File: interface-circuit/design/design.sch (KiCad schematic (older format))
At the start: 3 parts

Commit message: WIP
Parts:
- removed J?: Screw_Terminal_01x04, symbol Connector:Screw_Terminal_01x04
- added J?: Conn_02x06_Counter_Clockwise, symbol Connector_Generic:Conn_02x06_Counter_Clockwise
- added J?: Conn_02x15_Counter_Clockwise, symbol Connector_Generic:Conn_02x15_Counter_Clockwise
- added J? (x2): Conn_01x02_Male, symbol Connector:Conn_01x02_Male
- added J? (x2): Screw_Terminal_01x05, symbol Connector:Screw_Terminal_01x05
- added SW? (x2): SW_SPST, symbol Switch:SW_SPST
- added U?: LogicLevelConverter_BOB-08745, symbol custom_symbols:LogicLevelConverter_BOB-08745
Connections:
- net labels added: +12V, +3V3, +5V, HV_AlarmTriggered, HV_FanPowerDemand, HV_PrinterPowerDemand, HV_PrinterPowerStatus, LV_AlarmTriggered, LV_FanPowerDemand, LV_PrinterPowerDemand, LV_PrinterPowerStatus, RESET, SOFT_SWITCH
- net labels removed: ArduinoAlarmTriggered, ArduinoPrinterPowerStatus, PiPrinterPowerDemand
- wire segments 0 -> 28
- no-connect marks 36 -> 60

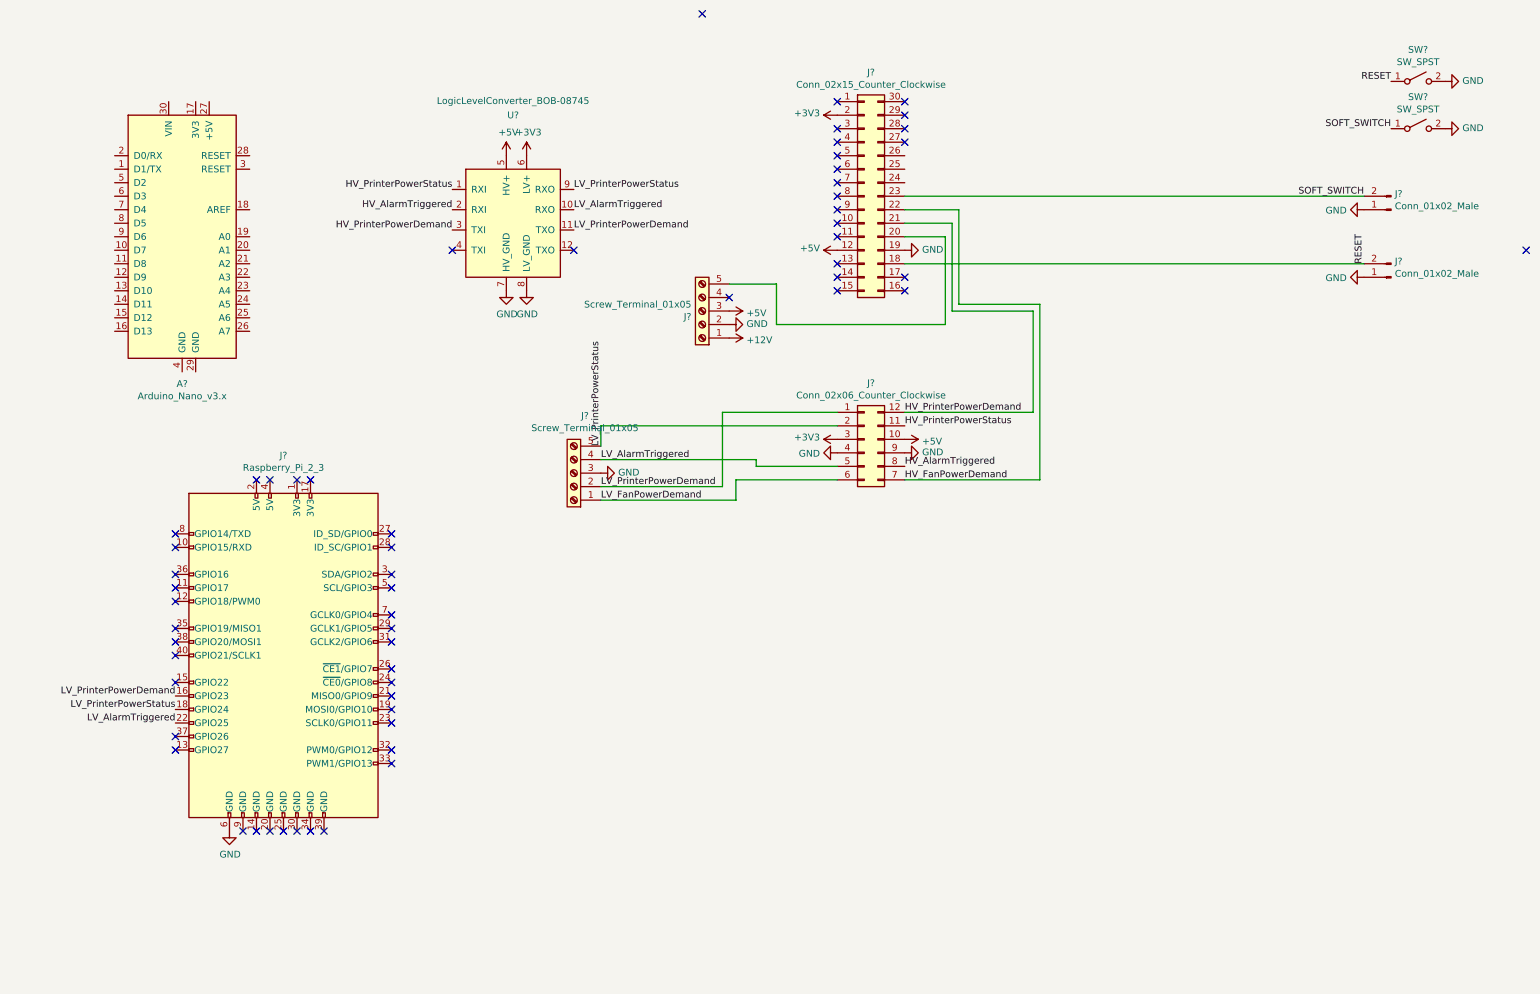
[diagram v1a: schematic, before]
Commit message: wip - transistor switches done
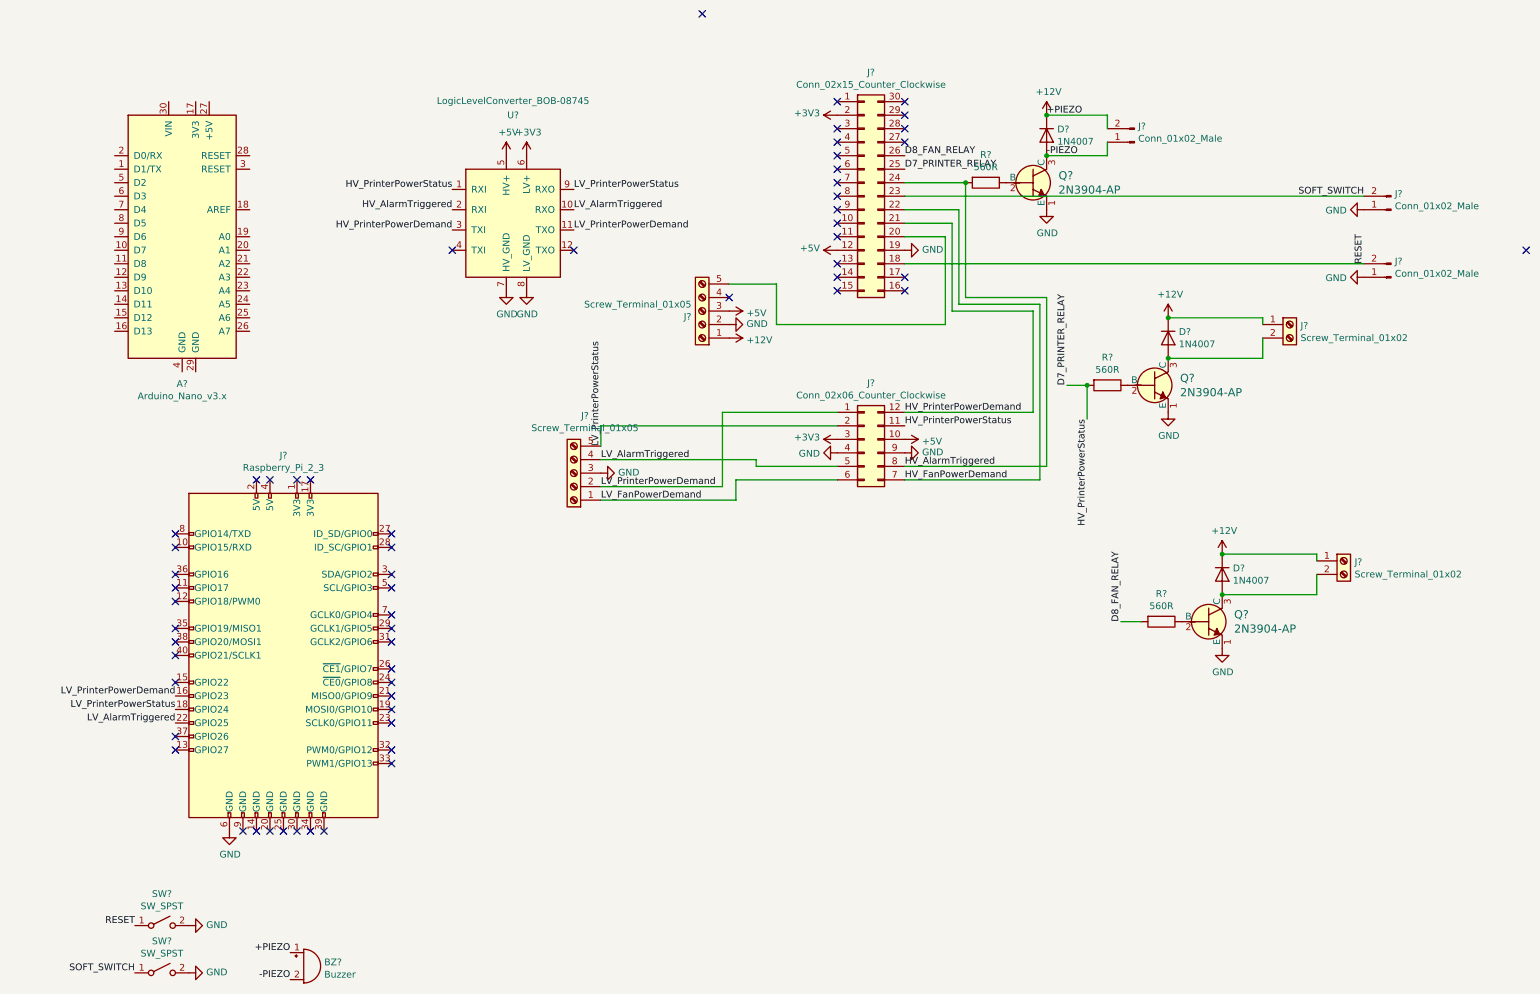
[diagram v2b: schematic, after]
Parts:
- added BZ?: Buzzer, symbol Device:Buzzer
- added D? (x3): 1N4007, Diode_THT:D_DO-41_SOD81_P10.16mm_Horizontal, symbol Diode:1N4007
- added J?: Conn_01x02_Male, symbol Connector:Conn_01x02_Male
- added J? (x2): Screw_Terminal_01x02, symbol Connector:Screw_Terminal_01x02
- added Q? (x3): 2N3904-AP, digikey-footprints:TO-92-3_Formed_Leads, symbol dk_Transistors-Bipolar-BJT-Single:2N3904-AP
- added R? (x3): 560R, symbol Device:R
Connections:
- net HV_PrinterPowerStatus is gone; now on net D7_PRINTER_RELAY: J?.11 (Pin_11), U?.1 (RXI)
- net +12V: now also BZ?.1 (-), D?.1 (K), D?.1 (K), D?.1 (K), J?.1 (Pin_1), J?.1 (Pin_1), J?.2 (Pin_2)
- net GND: now also Q?.1 (E), Q?.1 (E), Q?.1 (E)
- net HV_AlarmTriggered: now also J?.24 (Pin_24), R?.2
- net D7_PRINTER_RELAY: now reaches J?.25 (Pin_25)
- net D7_PRINTER_RELAY: now also R?.2
- net D8_FAN_RELAY: now reaches J?.26 (Pin_26)
- net D8_FAN_RELAY: now also R?.2
- new net: Q?.2 (B), R?.1 (x3)
- new net: D?.2 (A), J?.2 (Pin_2), Q?.3 (C) (x2)
- new net -PIEZO: BZ?.2 (+), D?.2 (A), J?.1 (Pin_1), Q?.3 (C)
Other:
- moved on the sheet: SW?

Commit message: Terminals for three-way switches, and 12v adaptor
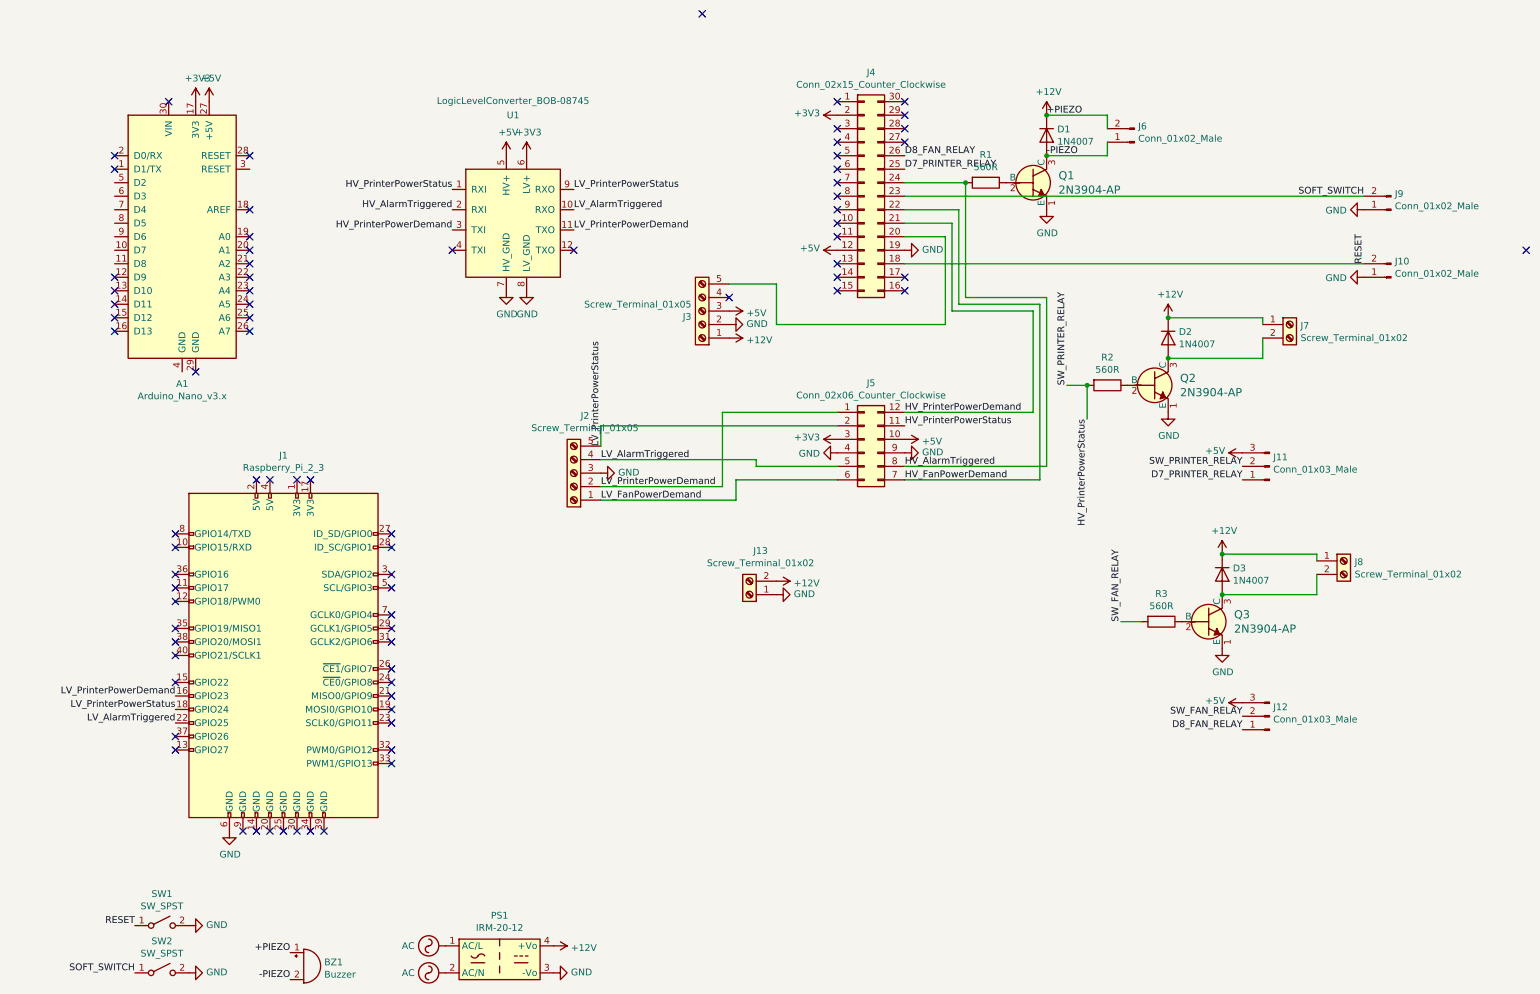
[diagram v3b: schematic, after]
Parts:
- added J11, J12: Conn_01x03_Male, symbol Connector:Conn_01x03_Male
- added J13: Screw_Terminal_01x02, symbol Connector:Screw_Terminal_01x02
- added PS1: IRM-20-12, Converter_ACDC:Converter_ACDC_MeanWell_IRM-20-xx_THT, symbol Converter_ACDC:IRM-20-12
- gave numbers to parts that had none: 24
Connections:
- net +12V: now also J13.2 (Pin_2), PS1.4 (+Vo)
- net +3V3: now also A1.17 (3V3)
- net +5V: now also A1.27 (+5V), J11.3 (Pin_3), J12.3 (Pin_3)
- net D7_PRINTER_RELAY: now also J11.1 (Pin_1); no longer J5.11 (Pin_11), R2.2, U1.1 (RXI)
- net D8_FAN_RELAY: now also J12.1 (Pin_1); no longer R3.2
- net GND: now also J13.1 (Pin_1), PS1.3 (-Vo)
- new net AC: PS1.1 (AC/L), PS1.2 (AC/N)
- new net HV_PrinterPowerStatus: J11.2 (Pin_2), J5.11 (Pin_11), R2.2, U1.1 (RXI)
- new net SW_FAN_RELAY: J12.2 (Pin_2), R3.2
- no-connect marks 60 -> 79

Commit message: Finished design and ERC passes
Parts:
- added J14: Conn_01x02_Male, symbol Connector:Conn_01x02_Male
- added R4: 220R, symbol Device:R
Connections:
- net +5V: now also R4.2
- net GND: now also A1.4 (GND), J14.1 (Pin_1)
- net HV_AlarmTriggered: now also A1.9 (D6)
- net HV_FanPowerDemand: now also A1.7 (D4)
- net HV_PrinterPowerDemand: now also A1.6 (D3)
- net HV_PrinterPowerStatus: now also A1.10 (D7)
- net RESET: now also A1.3 (RESET)
- net SOFT_SWITCH: now also A1.8 (D5)
- net SW_FAN_RELAY: now also A1.11 (D8)
- net DETECTOR_SIGNAL: now reaches A1.5 (D2)
- net DETECTOR_SIGNAL: now also J3.5 (Pin_5), J4.20 (Pin_20)
- net AC: no longer names the net of PS1.1 (AC/L)
- net AC: no longer PS1.2 (AC/N)
- new net: J14.2 (Pin_2), R4.1
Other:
- moved on the sheet: A1
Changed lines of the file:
@@
 L MCU_Module:Arduino_Nano_v3.x A1
 U 1 1 5CC13554
-P 1550 1950
-F 0 "A1" H 1550 861 50  0000 C CNN
-F 1 "Arduino_Nano_v3.x" H 1550 770 50  0000 C CNN
-F 2 "Module:Arduino_Nano" H 1700 1000 50  0001 L CNN
-F 3 "http://www.mouser.com/pdfdocs/Gravitech_Arduino_Nano3_0.pdf" H 1550 950 50  0001 C CNN
-	1    1550 1950
+P 2000 1700
+F 0 "A1" H 2000 611 50  0000 C CNN
+F 1 "Arduino_Nano_v3.x" H 2000 520 50  0000 C CNN
+F 2 "Module:Arduino_Nano" H 2150 750 50  0001 L CNN
+F 3 "http://www.mouser.com/pdfdocs/Gravitech_Arduino_Nano3_0.pdf" H 2000 700 50  0001 C CNN
+	1    2000 1700
 	1    0    0    -1
 $EndComp
@@
 $EndComp
 Connection ~ 9250 4300
-NoConn ~ 2050 1950
-NoConn ~ 2050 2050
-NoConn ~ 2050 2150
-NoConn ~ 2050 2250
-NoConn ~ 2050 2350
-NoConn ~ 2050 2450
-NoConn ~ 2050 2550
-NoConn ~ 2050 2650
-NoConn ~ 1450 950
-NoConn ~ 2050 1350
-NoConn ~ 2050 1750
-NoConn ~ 1650 2950
-NoConn ~ 1050 1350
-NoConn ~ 1050 1450
-NoConn ~ 1050 2250
-NoConn ~ 1050 2350
-NoConn ~ 1050 2450
-NoConn ~ 1050 2550
-NoConn ~ 1050 2650
+NoConn ~ 2500 1700
+NoConn ~ 2500 1800
+NoConn ~ 2500 1900
+NoConn ~ 2500 2000
+NoConn ~ 2500 2100
+NoConn ~ 2500 2200
+NoConn ~ 2500 2300
+NoConn ~ 2500 2400
+NoConn ~ 1900 700
+NoConn ~ 2500 1100
+NoConn ~ 2500 1500
+NoConn ~ 2100 2700
+NoConn ~ 1500 1100
+NoConn ~ 1500 1200
+NoConn ~ 1500 2000
+NoConn ~ 1500 2100
+NoConn ~ 1500 2200
+NoConn ~ 1500 2300
+NoConn ~ 1500 2400
 $Comp
 L power:+3V3 #PWR0127
 U 1 1 5CCA5351
-P 1650 950
-F 0 "#PWR0127" H 1650 800 50  0001 C CNN
-F 1 "+3V3" H 1665 1123 50  0000 C CNN
-F 2 "" H 1650 950 50  0001 C CNN
-F 3 "" H 1650 950 50  0001 C CNN
-	1    1650 950
+P 2100 700
+F 0 "#PWR0127" H 2100 550 50  0001 C CNN
+F 1 "+3V3" H 2115 873 50  0000 C CNN
+F 2 "" H 2100 700 50  0001 C CNN
+F 3 "" H 2100 700 50  0001 C CNN
+	1    2100 700
 	1    0    0    -1
 $EndComp
@@
 L power:+5V #PWR0128
 U 1 1 5CCA5F2D
-P 1750 950
-F 0 "#PWR0128" H 1750 800 50  0001 C CNN
-F 1 "+5V" H 1765 1123 50  0000 C CNN
-F 2 "" H 1750 950 50  0001 C CNN
-F 3 "" H 1750 950 50  0001 C CNN
-	1    1750 950
+P 2200 700
+F 0 "#PWR0128" H 2200 550 50  0001 C CNN
+F 1 "+5V" H 2215 873 50  0000 C CNN
+F 2 "" H 2200 700 50  0001 C CNN
+F 3 "" H 2200 700 50  0001 C CNN
+	1    2200 700
 	1    0    0    -1
 $EndComp
@@
 $EndComp
 $Comp
-L power:AC #PWR02
-U 1 1 5CCE518E
-P 3500 7200
-F 0 "#PWR02" H 3500 7100 50  0001 C CNN
-F 1 "AC" V 3500 7429 50  0000 L CNN
-F 2 "" H 3500 7200 50  0001 C CNN
-F 3 "" H 3500 7200 50  0001 C CNN
-	1    3500 7200
-	0    -1   -1   0
-$EndComp
-$Comp
-L power:AC #PWR03
-U 1 1 5CCE594D
-P 3500 7400
-F 0 "#PWR03" H 3500 7300 50  0001 C CNN
-F 1 "AC" V 3500 7629 50  0000 L CNN
-F 2 "" H 3500 7400 50  0001 C CNN
-F 3 "" H 3500 7400 50  0001 C CNN
-	1    3500 7400
-	0    -1   -1   0
-$EndComp
-$Comp
 L Connector:Screw_Terminal_01x02 J13
 U 1 1 5CCF3969
@@
 	0    -1   -1   0
 $EndComp
+$Comp
+L Device:R R4
+U 1 1 5CC3D025
+P 6950 4900
+F 0 "R4" V 6743 4900 50  0000 C CNN
+F 1 "220R" V 6834 4900 50  0000 C CNN
+F 2 "" V 6880 4900 50  0001 C CNN
+F 3 "~" H 6950 4900 50  0001 C CNN
+	1    6950 4900
+	0    1    1    0
+$EndComp
+$Comp
+L Connector:Conn_01x02_Male J14
+U 1 1 5CC3E12C
+P 7300 5000
+F 0 "J14" H 7272 4882 50  0000 R CNN
+F 1 "Conn_01x02_Male" H 7272 4973 50  0000 R CNN
+F 2 "" H 7300 5000 50  0001 C CNN
+F 3 "~" H 7300 5000 50  0001 C CNN
+	1    7300 5000
+	-1   0    0    1
+$EndComp
+$Comp
+L power:GND #PWR09
+U 1 1 5CC3F099
+P 7100 5000
+F 0 "#PWR09" H 7100 4750 50  0001 C CNN
+F 1 "GND" H 7105 4827 50  0000 C CNN
+F 2 "" H 7100 5000 50  0001 C CNN
+F 3 "" H 7100 5000 50  0001 C CNN
+	1    7100 5000
+	1    0    0    -1
+$EndComp
+$Comp
+L power:+5V #PWR08
+U 1 1 5CC40612
+P 6800 4900
+F 0 "#PWR08" H 6800 4750 50  0001 C CNN
+F 1 "+5V" V 6815 5028 50  0000 L CNN
+F 2 "" H 6800 4900 50  0001 C CNN
+F 3 "" H 6800 4900 50  0001 C CNN
+	1    6800 4900
+	0    -1   -1   0
+$EndComp
+Text Label 2500 1200 0    50   ~ 0
+RESET
+Text Label 1500 1400 2    50   ~ 0
+HV_PrinterPowerDemand
+Text Label 1500 1500 2    50   ~ 0
+HV_FanPowerDemand
+Text Label 1500 1600 2    50   ~ 0
+SOFT_SWITCH
+Text Label 1500 1700 2    50   ~ 0
+HV_AlarmTriggered
+Text Label 1500 1800 2    50   ~ 0
+SW_PRINTER_RELAY
+Text Label 1500 1900 2    50   ~ 0
+SW_FAN_RELAY
+$Comp
+L power:GND #PWR0132
+U 1 1 5CC65335
+P 2000 2700
+F 0 "#PWR0132" H 2000 2450 50  0001 C CNN
+F 1 "GND" H 2005 2527 50  0000 C CNN
+F 2 "" H 2000 2700 50  0001 C CNN
+F 3 "" H 2000 2700 50  0001 C CNN
+	1    2000 2700
+	1    0    0    -1
+$EndComp
+Text Label 1500 1300 2    50   ~ 0
+DETECTOR_SIGNAL
+Text Label 5600 2300 0    50   ~ 0
+DETECTOR_SIGNAL
+$Comp
+L power:PWR_FLAG #FLG0101
+U 1 1 5CC7D054
+P 3500 7200
+F 0 "#FLG0101" H 3500 7275 50  0001 C CNN
+F 1 "PWR_FLAG" V 3500 7327 50  0000 L CNN
+F 2 "" H 3500 7200 50  0001 C CNN
+F 3 "~" H 3500 7200 50  0001 C CNN
+	1    3500 7200
+	0    -1   -1   0
+$EndComp
+$Comp
+L power:PWR_FLAG #FLG0102
+U 1 1 5CC7DA6D
+P 3500 7400
+F 0 "#FLG0102" H 3500 7475 50  0001 C CNN
+F 1 "PWR_FLAG" V 3500 7527 50  0000 L CNN
+F 2 "" H 3500 7400 50  0001 C CNN
+F 3 "~" H 3500 7400 50  0001 C CNN
+	1    3500 7400
+	0    -1   -1   0
+$EndComp
